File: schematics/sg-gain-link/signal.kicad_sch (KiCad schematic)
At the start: 16 parts, among them U3 OPA1612AxD, U4 INA849D

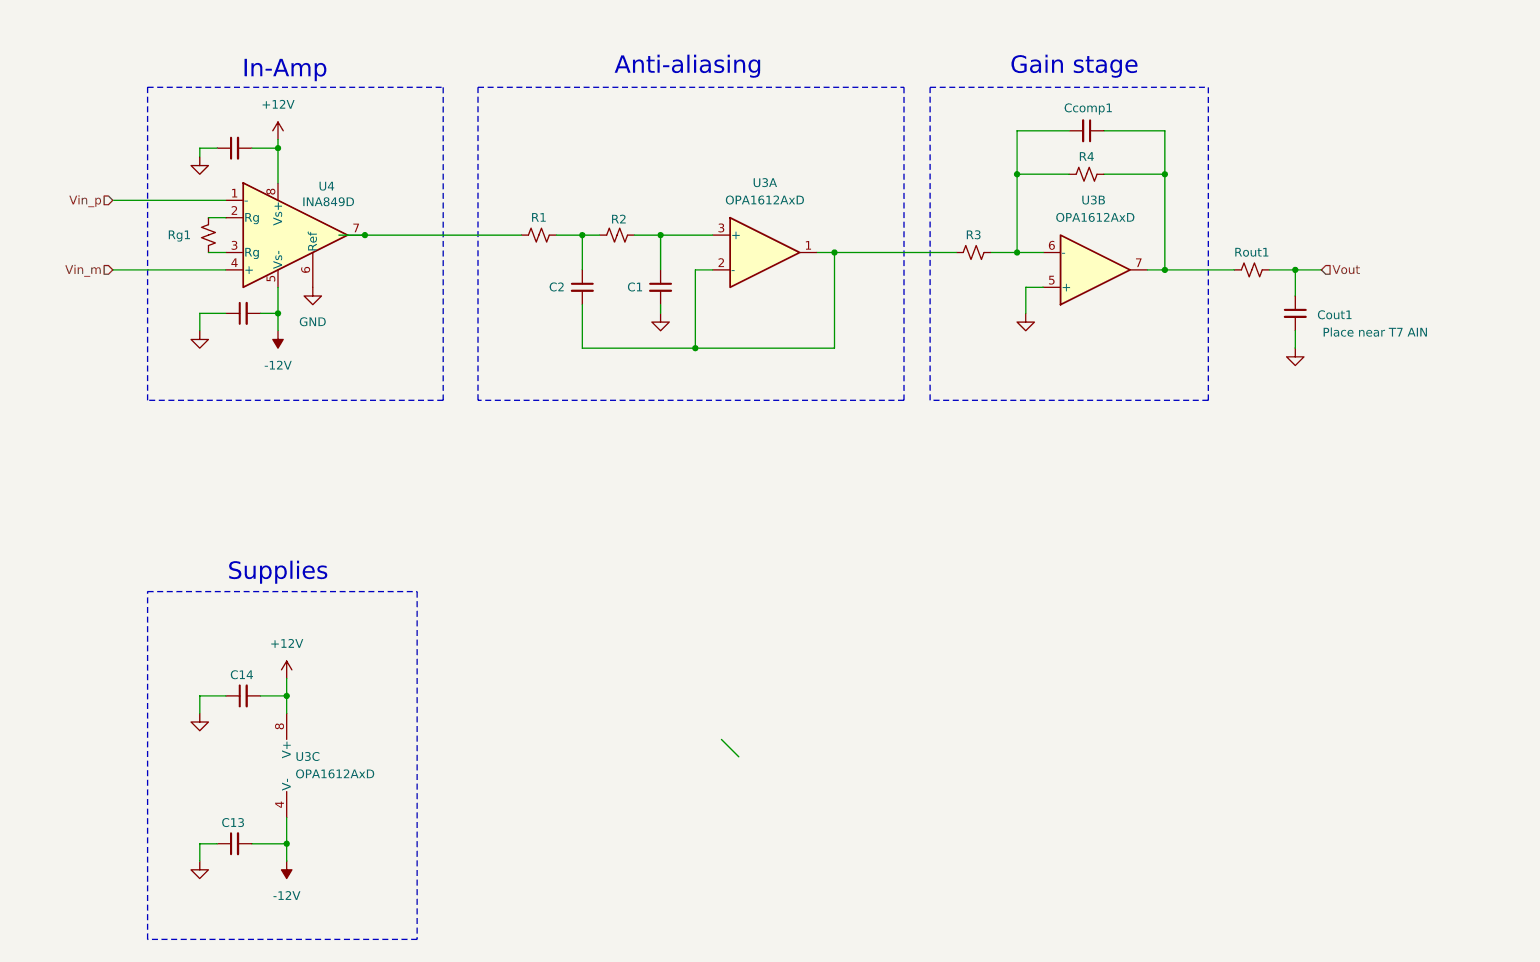
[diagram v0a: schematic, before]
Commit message: update naming, jlc standards, and add text
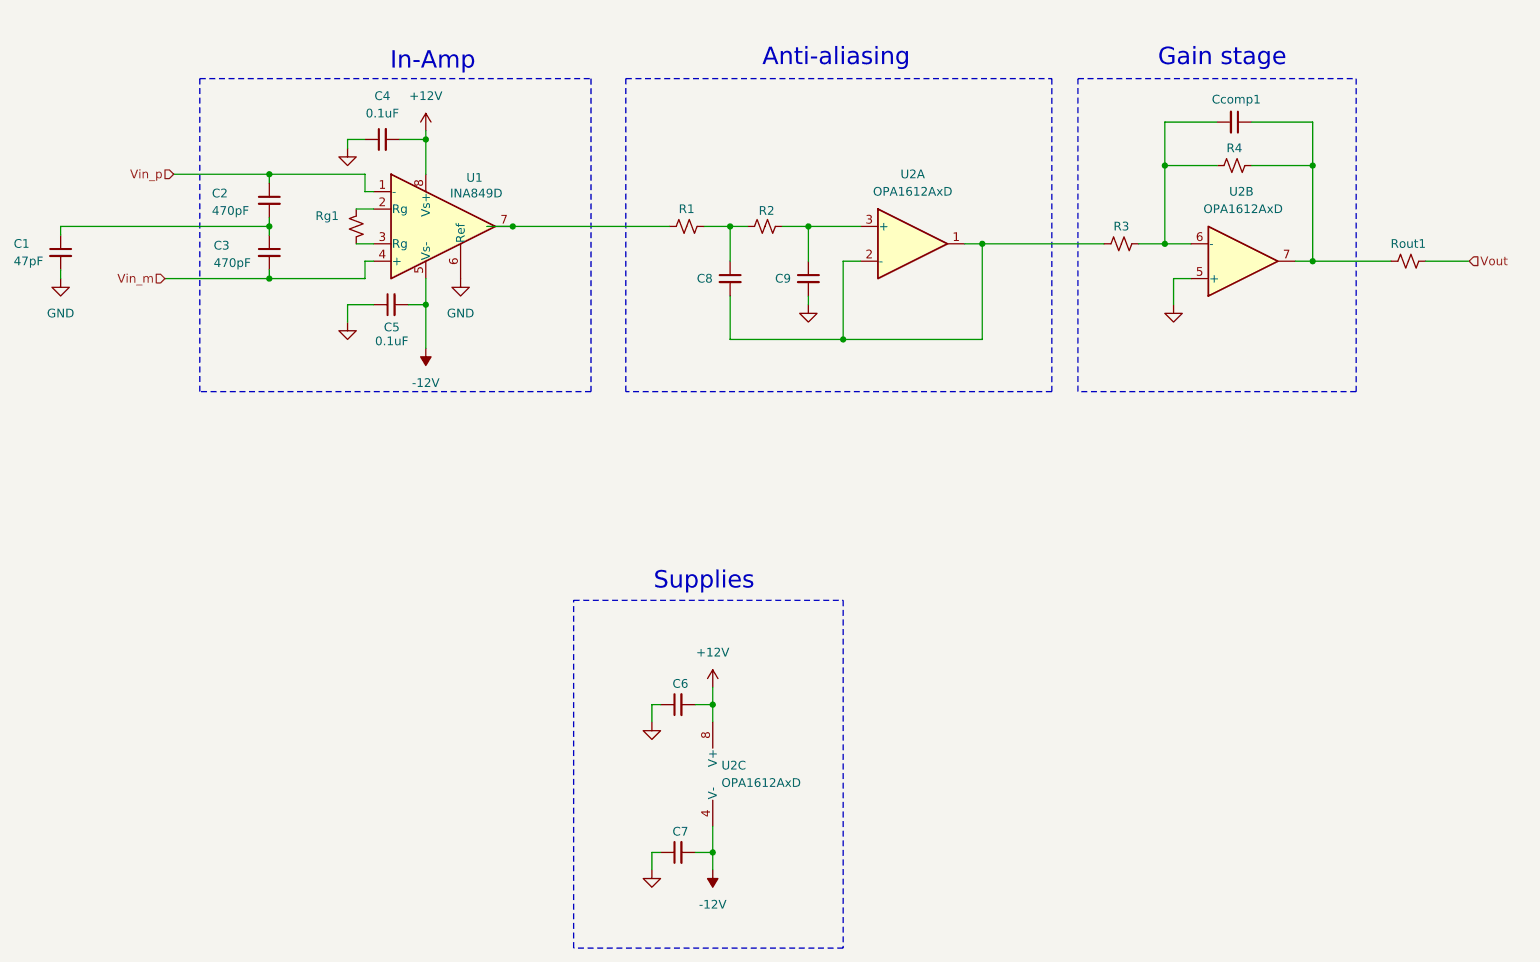
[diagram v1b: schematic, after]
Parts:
- removed Cout1: C_Small, symbol Device:C_Small
- added C1: 47pF, Capacitor_SMD:C_0402_1005Metric, symbol Device:C_Small
- added C2, C3: 470pF, Capacitor_SMD:C_0402_1005Metric, symbol Device:C_Small
- C4: renamed from C16; value C_Small -> 0.1uF; footprint (none) -> Capacitor_SMD:C_0402_1005Metric
- C5: renamed from C15; value C_Small -> 0.1uF; footprint (none) -> Capacitor_SMD:C_0402_1005Metric
- C6: renamed from C14; footprint (none) -> Capacitor_SMD:C_0402_1005Metric
- C7: renamed from C13; footprint (none) -> Capacitor_SMD:C_0402_1005Metric
- C8: renamed from C2; footprint (none) -> Capacitor_SMD:C_0402_1005Metric
- C9: renamed from C1; footprint (none) -> Capacitor_SMD:C_0402_1005Metric
- Ccomp1: footprint (none) -> Capacitor_SMD:C_0402_1005Metric
- R1, R2, R3, R4, Rg1, Rout1: footprint (none) -> Resistor_SMD:R_0805_2012Metric
- U2: renamed from U3; footprint (none) -> Link_Footprints:OPA1612
- renumbered U4 to U1
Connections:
- net GND: now also C1.2
- net Vin_m: now also C3.2
- net Vin_p: now also C2.1
- new net: C1.1, C2.2, C3.1
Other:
- moved on the sheet: C6, C7, C8, C9, Ccomp1, R1, R2, R3, R4, Rg1, Rout1, U1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

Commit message: update board
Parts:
- R1, R2, R3, R4, Rg1, Rout1: footprint Resistor_SMD:R_0805_2012Metric -> Resistor_SMD:R_0603_1608Metric
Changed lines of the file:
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@@
 			)
 		)
-		(property "Footprint" "Resistor_SMD:R_0805_2012Metric"
+		(property "Footprint" "Resistor_SMD:R_0603_1608Metric"
 			(at 198.12 66.04 0)
 			(effects
@@
 			)
 		)
-		(property "Footprint" "Resistor_SMD:R_0805_2012Metric"
+		(property "Footprint" "Resistor_SMD:R_0603_1608Metric"
 			(at 214.63 54.61 0)
 			(effects
@@
 			)
 		)
-		(property "Footprint" "Resistor_SMD:R_0805_2012Metric"
+		(property "Footprint" "Resistor_SMD:R_0603_1608Metric"
 			(at 146.05 63.5 0)
 			(effects
@@
 			)
 		)
-		(property "Footprint" "Resistor_SMD:R_0805_2012Metric"
+		(property "Footprint" "Resistor_SMD:R_0603_1608Metric"
 			(at 134.62 63.5 0)
 			(effects
@@
 			)
 		)
-		(property "Footprint" "Resistor_SMD:R_0805_2012Metric"
+		(property "Footprint" "Resistor_SMD:R_0603_1608Metric"
 			(at 240.03 68.58 0)
 			(effects
@@
 			)
 		)
-		(property "Footprint" "Resistor_SMD:R_0805_2012Metric"
+		(property "Footprint" "Resistor_SMD:R_0603_1608Metric"
 			(at 86.36 63.5 0)
 			(effects

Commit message: update sg-gain-link
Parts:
- C6, C7: value C_Small -> 0.1uF
- C8: value C_Small -> 2.7nF
- C9: value C_Small -> 5.6nF
- Ccomp1: value C_Small -> 33pF
- R1, R2: value R_Small_US -> 3.3k
- R3, R4: value R_Small_US -> 1k
- Rg1: value R_Small_US -> 121
- Rout1: value R_Small_US -> 49.9
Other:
- note added: ".ac DEC 10 10 1Meg"
- moved on the sheet: C6, C7, Ccomp1, R3, R4, Rout1, U2B

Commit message: release(sg-link): v1.0. Sent for production.
Signed-off-by: Andrew Balmos <abalmos@purdue.edu>
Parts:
- added R10, R9: 499, Resistor_SMD:R_0603_1608Metric, symbol Device:R_Small_US
- C1: footprint Capacitor_SMD:C_0402_1005Metric -> Capacitor_SMD:C_0603_1608Metric; LCSC (none) -> C519486; MPN (none) -> CC0603FRNPO9BN470
- C2: renamed from C3; footprint Capacitor_SMD:C_0402_1005Metric -> Capacitor_SMD:C_0603_1608Metric; LCSC (none) -> C519564; MPN (none) -> CC0603FRNPO9BN471
- C27: renamed from Ccomp1; footprint Capacitor_SMD:C_0402_1005Metric -> Capacitor_SMD:C_0603_1608Metric; LCSC (none) -> C519485; MPN (none) -> CC0603FRNPO9BN330
- C3: renamed from C2; footprint Capacitor_SMD:C_0402_1005Metric -> Capacitor_SMD:C_0603_1608Metric; LCSC (none) -> C519564; MPN (none) -> CC0603FRNPO9BN471
- C4, C5, C6, C7: value 0.1uF -> 100n; footprint Capacitor_SMD:C_0402_1005Metric -> Capacitor_SMD:C_0603_1608Metric; LCSC (none) -> C6119867; MPN (none) -> CGA0603X7R104K500JT
- C8: footprint Capacitor_SMD:C_0402_1005Metric -> Capacitor_SMD:C_1206_3216Metric; LCSC (none) -> C541595; MPN (none) -> CC1206FRNPO9BN272
- C9: footprint Capacitor_SMD:C_0402_1005Metric -> Capacitor_SMD:C_0603_1608Metric; LCSC (none) -> C327284; MPN (none) -> CC0603DRNPO9BN5R6
- R1, R2: LCSC (none) -> C22356670; MPN (none) -> RCA033K3JLF
- R16: renamed from Rout1; LCSC (none) -> C22369800; MPN (none) -> RCA0349R9FLF
- R3, R4: LCSC (none) -> C22356624; MPN (none) -> RCA031KJLF
- Rg1: LCSC (none) -> C705721; MPN (none) -> RT0603BRD07121RL
- U1: LCSC (none) -> C2871861; MPN (none) -> INA849DR
- U2: footprint Link_Footprints:OPA1612 -> Package_SO:SOIC-8_5.3x6.2mm_P1.27mm; LCSC (none) -> C94590; MPN (none) -> OPA1612AIDR
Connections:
- net Vin_m: now also R10.1; no longer C2.2, U1.4 (+)
- net Vin_p: now also R9.1; no longer C3.1, U1.1 (-)
- new net: C2.2, R9.2, U1.4 (+)
- new net: C3.1, R10.2, U1.1 (-)
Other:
- moved on the sheet: C1
